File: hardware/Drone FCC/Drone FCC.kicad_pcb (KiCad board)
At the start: 2 copper layers, 80 x 62.2 mm, 36 parts, among them J1 Mag Dupont, J10 Conn_01x03, J11 Conn_01x03, J12 Conn_01x03, J13 Conn_01x03, J14 Conn_01x03, J17 Conn_01x03, J18 Conn_01x03, J19 GPS M8N - DF13, J2 GPS Dupont, J20 Mag DF13, J21 Micro_SD_Card_Det_Hirose_DM3AT, J22 Conn_02x03_Counter_Clockwise, J23 Conn_01x03, J24 DSM Spektrum JST, J25 105017-0001, J26 Conn_01x03, J27 PPM Dupont, J28 PM02 PixHawk, J3 Conn_01x03, J4 Conn_01x03, J5 Conn_01x03, J6 Conn_01x03, J7 Conn_01x03, J8 Conn_01x03, J9 Conn_01x03, SW1 SW_MEC_5E, U1 ICM-42688-V, U2 ILPS22QSTR, U3 STM32F746ZGTx, U4 SN65HVD230, U5 SN65HVD230, U6 ZLDO1117QG33TA, U7 USBLC6-2SC6

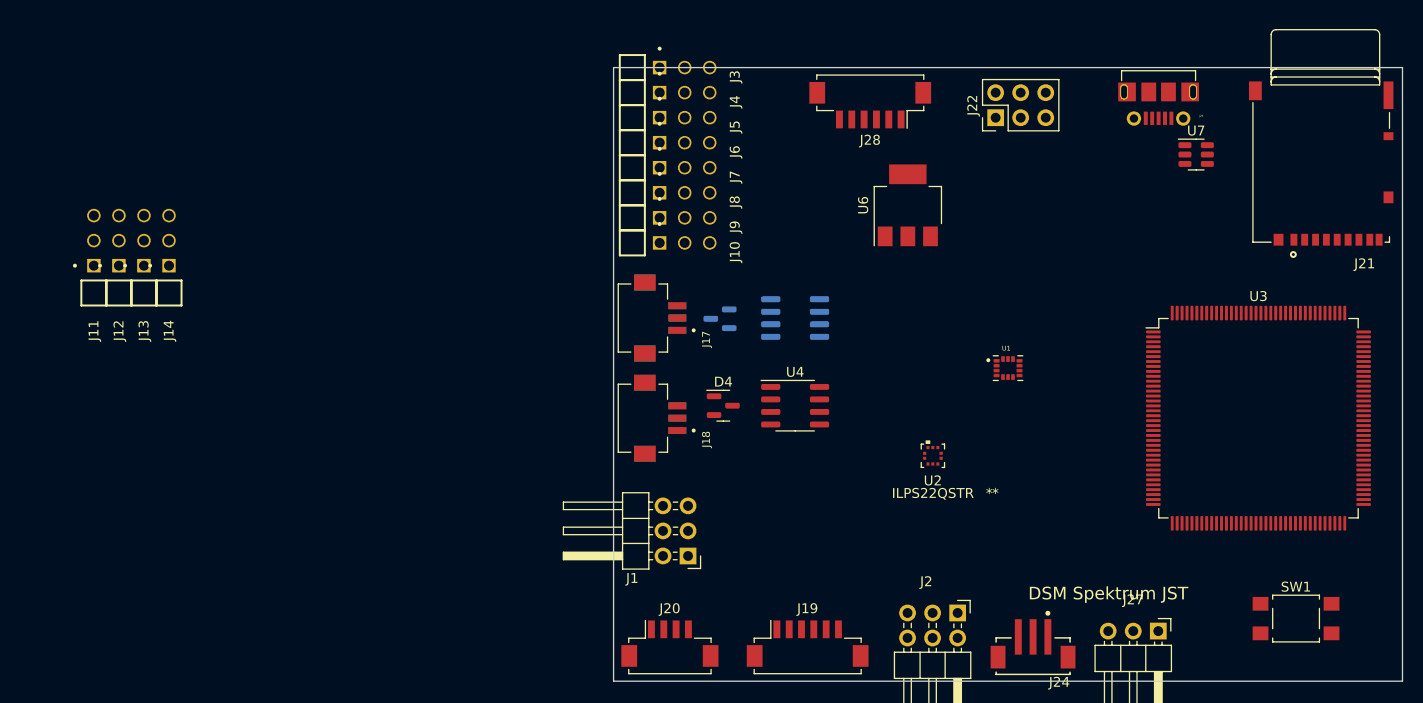
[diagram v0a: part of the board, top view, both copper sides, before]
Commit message: add external communication connectors
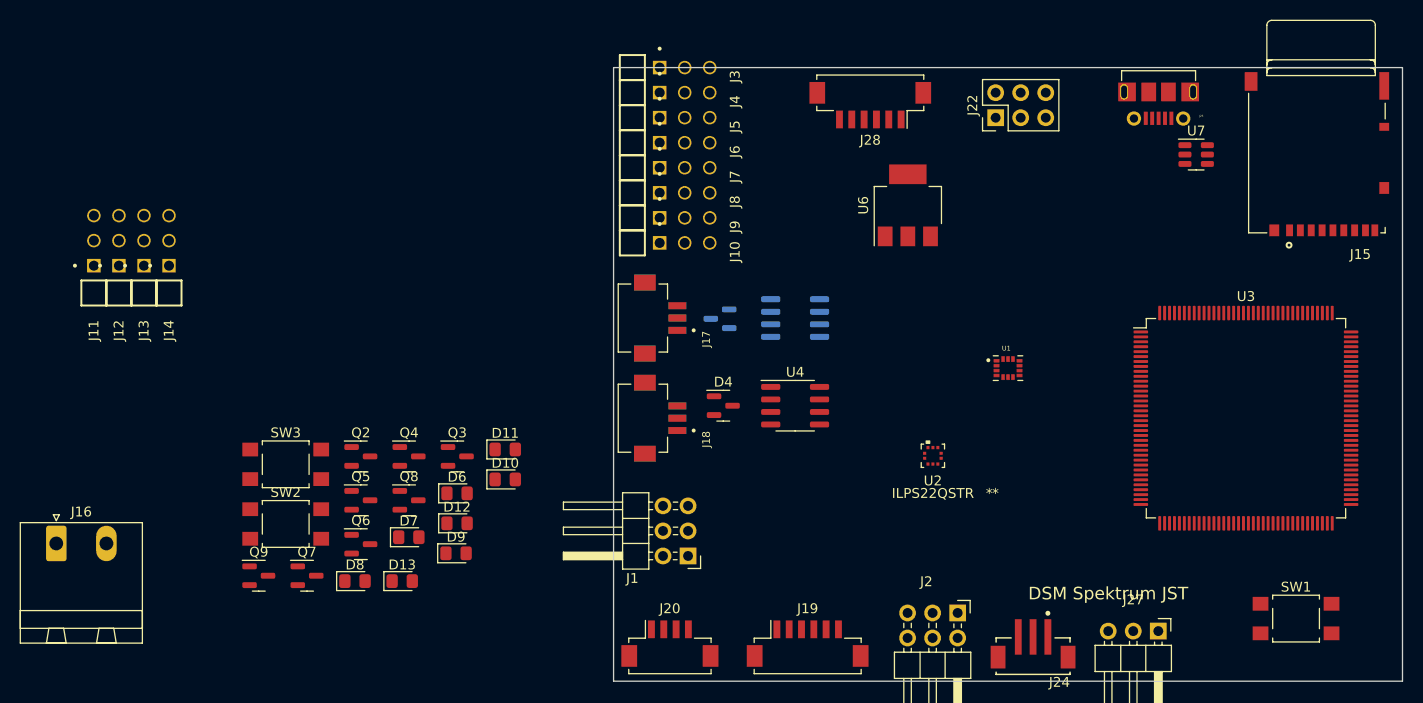
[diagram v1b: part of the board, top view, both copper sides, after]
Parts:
- removed J21: Micro_SD_Card_Det_Hirose_DM3AT, DM3AT-SF-PEJM5:HRS_DM3AT-SF-PEJM5
- added D10: LED_BLUE, LED_SMD:LED_0805_2012Metric_Pad1.15x1.40mm_HandSolder, F.Cu at (104.0, 101.5)
- added D11: LED_BLUE, LED_SMD:LED_0805_2012Metric_Pad1.15x1.40mm_HandSolder, F.Cu at (104.0, 98.4)
- added D12: LED_YELLOW, LED_SMD:LED_0805_2012Metric_Pad1.15x1.40mm_HandSolder, F.Cu at (99.1, 105.9)
- added D13: LED_YELLOW, LED_SMD:LED_0805_2012Metric_Pad1.15x1.40mm_HandSolder, F.Cu at (93.5, 111.8)
- added D6: LED_RED, LED_SMD:LED_0805_2012Metric_Pad1.15x1.40mm_HandSolder, F.Cu at (99.1, 102.9)
- added D7: LED_GREEN, LED_SMD:LED_0805_2012Metric_Pad1.15x1.40mm_HandSolder, F.Cu at (94.2, 107.3)
- added D8: LED_RED, LED_SMD:LED_0805_2012Metric_Pad1.15x1.40mm_HandSolder, F.Cu at (88.7, 111.8)
- added D9: LED_GREEN, LED_SMD:LED_0805_2012Metric_Pad1.15x1.40mm_HandSolder, F.Cu at (99.0, 109.0)
- added J15: DM3AT-SF-PEJM5, DM3AT-SF-PEJM5:HRS_DM3AT-SF-PEJM5, F.Cu at (186.7, 76.2)
- added J16: Conn_01x02, Connector_Phoenix_MSTB:PhoenixContact_MSTBA_2,5_2-G-5,08_1x02_P5.08mm_Horizontal, F.Cu at (58.4, 108.0)
- added Q2: 2N7002, Package_TO_SOT_SMD:SOT-23, F.Cu at (89.3, 99.1)
- added Q3: 2N7002, Package_TO_SOT_SMD:SOT-23, F.Cu at (99.1, 99.1)
- added Q4: 2N7002, Package_TO_SOT_SMD:SOT-23, F.Cu at (94.2, 99.1)
- added Q5: 2N7002, Package_TO_SOT_SMD:SOT-23, F.Cu at (89.3, 103.6)
- added Q6: 2N7002, Package_TO_SOT_SMD:SOT-23, F.Cu at (89.3, 108.0)
- added Q7: 2N7002, Package_TO_SOT_SMD:SOT-23, F.Cu at (83.8, 111.2)
- added Q8: 2N7002, Package_TO_SOT_SMD:SOT-23, F.Cu at (94.2, 103.6)
- added Q9: 2N7002, Package_TO_SOT_SMD:SOT-23, F.Cu at (79.0, 111.2)
- added SW2: SW_MEC_5E, Button_Switch_SMD:SW_SPST_TL3305A, F.Cu at (81.7, 106.0)
- added SW3: SW_MEC_5E, Button_Switch_SMD:SW_SPST_TL3305A, F.Cu at (81.7, 99.9)
- moved U3 1.27 mm to (179.1, 95.2)
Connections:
- J10 pad 1: /Motores_servos_PWM/ESC_8 -> /MCU/TIM4_CH4
- J11 pad 1: /Motores_servos_PWM/SERVO_1 -> /MCU/TIM1_CH1
- J12 pad 1: /Motores_servos_PWM/SERVO_2 -> /MCU/TIM1_CH2
- J13 pad 1: /Motores_servos_PWM/SERVO_3 -> /MCU/TIM1_CH3
- J14 pad 1: /Motores_servos_PWM/SERVO_4 -> /MCU/TIM1_CH4
- J2 pad 6: /Sensores/GNSS_PPS -> /MCU/PD_10(EXTI10)
- J24 pad 3: /RC control/DSM_DATA -> /MCU/USART6_RX
- J27 pad 3: /RC control/PPM -> /MCU/TIM2_CH3
- J3 pad 1: /MCU/PWM1 -> /MCU/TIM3_CH1
- J4 pad 1: /MCU/PWM2 -> /MCU/TIM3_CH2
- J5 pad 1: /MCU/PWM3 -> /MCU/TIM3_CH3
- J6 pad 1: /MCU/PWM4 -> /MCU/TIM3_CH4
- J7 pad 1: /MCU/PWM8 -> /MCU/TIM4_CH1
- J8 pad 1: /MCU/PWM9 -> /MCU/TIM4_CH2
- J9 pad 1: /Motores_servos_PWM/ESC_7 -> /MCU/TIM4_CH3
- U1 pad 1: /MCU/SPI1_MISO -> /MCU/SPI5_MISO
- U1 pad 12: /Sensores/IMU_CS -> /MCU/SPI5_CS
- U1 pad 13: /MCU/SPI1_SCK -> /MCU/SPI5_SCK
- U1 pad 14: /MCU/SPI1_MOSI -> /MCU/SPI5_MOSI
- U1 pad 4: /Sensores/IMU_INT_DATA_RDY -> /MCU/PF_5(EXTI5)
- U2 pad 2: /MCU/I2C2_SCL -> /Sensores/GNSS_SCL
- U2 pad 4: /MCU/I2C2_SDA -> /Sensores/GNSS_SDA
- U3 pad 114: /Interfaz_CAN/CAN1_RX -> unconnected-(U3-Pad114)
- U3 pad 115: /Interfaz_CAN/CAN1_TX -> unconnected-(U3-Pad115)
- U3 pad 118: unconnected-(U3-Pad118) -> /MCU/PD_4(EXTI4)
- U3 pad 124: unconnected-(U3-Pad124) -> /MCU/USART6_RX
- U3 pad 137: unconnected-(U3-Pad137) -> /Interfaz_CAN/CAN2_MODE
- U3 pad 139: unconnected-(U3-Pad139) -> /Interfaz_CAN/CAN1_RX
- U3 pad 140: unconnected-(U3-Pad140) -> /Interfaz_CAN/CAN1_TX
- U3 pad 141: unconnected-(U3-Pad141) -> /Interfaz_CAN/CAN1_MODE
- U3 pad 15: unconnected-(U3-Pad15) -> /MCU/PF_5(EXTI5)
- U3 pad 18: unconnected-(U3-Pad18) -> /MCU/SPI5_CS
- U3 pad 19: unconnected-(U3-Pad19) -> /MCU/SPI5_SCK
- U3 pad 20: unconnected-(U3-Pad20) -> /MCU/SPI5_MISO
- U3 pad 21: unconnected-(U3-Pad21) -> /MCU/SPI5_MOSI
- U3 pad 28: unconnected-(U3-Pad28) -> /Alimentación/I_MEAS
- U3 pad 29: unconnected-(U3-Pad29) -> /Alimentación/V_MEAS
- U3 pad 36: unconnected-(U3-Pad36) -> /MCU/TIM2_CH3
- U3 pad 41: /MCU/SPI1_SCK -> unconnected-(U3-Pad41)
- U3 pad 42: /MCU/SPI1_MISO -> /MCU/TIM3_CH1
- U3 pad 43: /MCU/SPI1_MOSI -> /MCU/TIM3_CH2
- U3 pad 46: unconnected-(U3-Pad46) -> /MCU/TIM3_CH3
- U3 pad 47: unconnected-(U3-Pad47) -> /MCU/TIM3_CH4
- U3 pad 53: /MCU/I2C4_SMBA -> unconnected-(U3-Pad53)
- U3 pad 56: unconnected-(U3-Pad56) -> /Sensores/MAG_INT_DATA_RDY
- U3 pad 60: /MCU/PWM11 -> /MCU/TIM1_CH1
- U3 pad 64: /MCU/PWM10 -> /MCU/TIM1_CH2
- U3 pad 66: /MCU/PWM9 -> /MCU/TIM1_CH3
- U3 pad 67: /MCU/PWM8 -> /MCU/TIM1_CH4
- U3 pad 68: unconnected-(U3-Pad68) -> /MCU/PE_15(EXTI15)
- U3 pad 69: /MCU/I2C2_SCL -> /Sensores/GNSS_SCL
- U3 pad 7: /MCU/SD_SW -> unconnected-(U3-Pad7)
- U3 pad 70: /MCU/I2C2_SDA -> /Sensores/GNSS_SDA
- U3 pad 77: unconnected-(U3-Pad77) -> /Sensores/GNSS_Tx
- U3 pad 78: unconnected-(U3-Pad78) -> /Sensores/GNSS_Rx
- U3 pad 79: unconnected-(U3-Pad79) -> /MCU/PD_10(EXTI10)
- U3 pad 81: /MCU/PWM1 -> /MCU/TIM4_CH1
- U3 pad 82: /MCU/PWM2 -> /MCU/TIM4_CH2
- U3 pad 85: /MCU/PWM3 -> /MCU/TIM4_CH3
- U3 pad 86: /MCU/PWM4 -> /MCU/TIM4_CH4

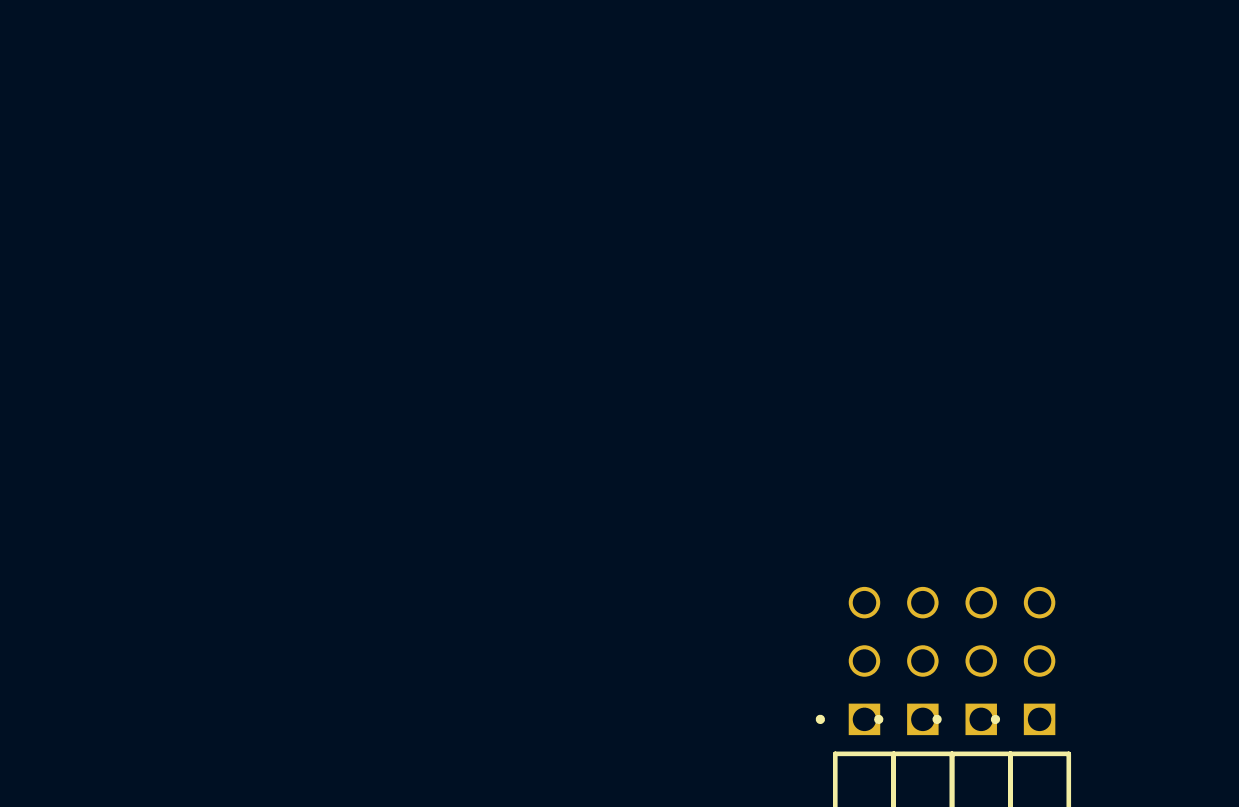
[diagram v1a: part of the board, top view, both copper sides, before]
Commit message: re enumeration of components
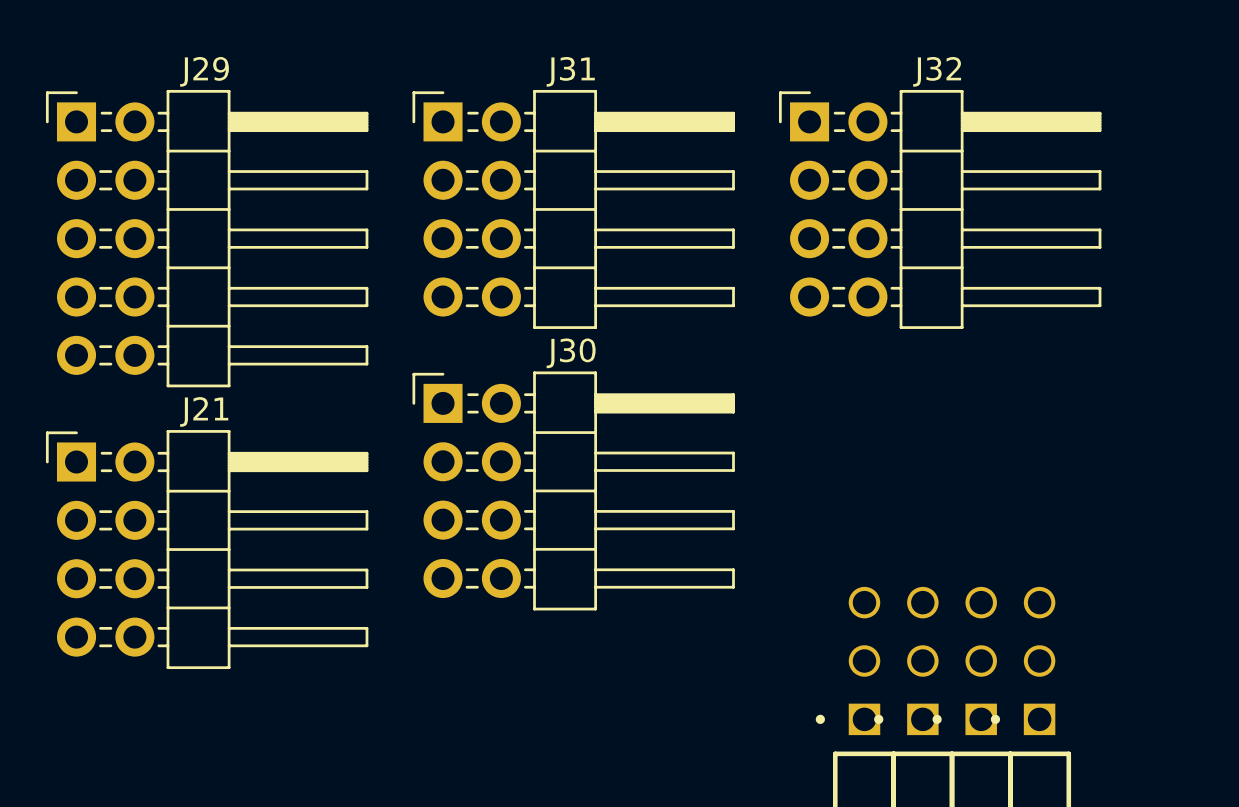
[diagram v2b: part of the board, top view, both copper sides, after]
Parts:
- added J21: SPI externo, Connector_PinHeader_2.54mm:PinHeader_2x04_P2.54mm_Horizontal, F.Cu at (27.9, 68.6)
- added J29: I2C externo x2, Connector_PinHeader_2.54mm:PinHeader_2x05_P2.54mm_Horizontal, F.Cu at (27.9, 53.8)
- added J30: UART externa x2, Connector_PinHeader_2.54mm:PinHeader_2x04_P2.54mm_Horizontal, F.Cu at (43.9, 66.0)
- added J31: UART externa x2, Connector_PinHeader_2.54mm:PinHeader_2x04_P2.54mm_Horizontal, F.Cu at (43.9, 53.8)
- added J32: 5V y 3V3 x 2, Connector_PinHeader_2.54mm:PinHeader_2x04_P2.54mm_Horizontal, F.Cu at (59.8, 53.8)
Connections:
- J24 pad 3: /MCU/USART6_RX -> /MCU/UART7_RX
- U3 pad 1: unconnected-(U3-Pad1) -> /Conexiones_extra/SPI_SCK
- U3 pad 110: unconnected-(U3-Pad110) -> /Interfaz_CAN/CAN1_MODE
- U3 pad 114: unconnected-(U3-Pad114) -> /Interfaz_CAN/CAN1_RX
- U3 pad 115: unconnected-(U3-Pad115) -> /Interfaz_CAN/CAN1_TX
- U3 pad 119: unconnected-(U3-Pad119) -> /Conexiones_extra/UARTB_TX
- U3 pad 122: unconnected-(U3-Pad122) -> /Conexiones_extra/UARTB_RX
- U3 pad 124: /MCU/USART6_RX -> /Conexiones_extra/UARTA_RX
- U3 pad 129: unconnected-(U3-Pad129) -> /Conexiones_extra/UARTA_TX
- U3 pad 139: /Interfaz_CAN/CAN1_RX -> /Conexiones_extra/I2CA_SCL
- U3 pad 140: /Interfaz_CAN/CAN1_TX -> /Conexiones_extra/I2CA_SDA
- U3 pad 141: /Interfaz_CAN/CAN1_MODE -> /Conexiones_extra/UARTD_RX
- U3 pad 142: unconnected-(U3-Pad142) -> /Conexiones_extra/UARTD_TX
- U3 pad 2: unconnected-(U3-Pad2) -> /Conexiones_extra/SPI_EOC
- U3 pad 3: unconnected-(U3-Pad3) -> /Conexiones_extra/SPI_CS
- U3 pad 34: unconnected-(U3-Pad34) -> /Conexiones_extra/UARTC_TX
- U3 pad 35: unconnected-(U3-Pad35) -> /Conexiones_extra/UARTC_RX
- U3 pad 4: unconnected-(U3-Pad4) -> /Conexiones_extra/SPI_MISO
- U3 pad 5: unconnected-(U3-Pad5) -> /Conexiones_extra/SPI_MOSI
- U3 pad 58: unconnected-(U3-Pad58) -> /MCU/UART7_RX

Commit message: start routing
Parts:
- removed J17, J18, J23, J26: Conn_01x03, DF13A-3P-1.25H(21):HRS_DF13A-3P-1.25H(21)
- removed J19: GPS M8N - DF13, Connector_Hirose:Hirose_DF13C_CL535-0406-3-51_1x06-1MP_P1.25mm_Vertical
- removed J20: Mag DF13, Connector_Hirose:Hirose_DF13C_CL535-0404-8-51_1x04-1MP_P1.25mm_Vertical
- removed J24: DSM Spektrum JST, B3B-ZR-SM4-TF(LF)(SN):JST-B3B-ZR-SM4-TFLFSN-0-0-MFG
- removed J25: 105017-0001, 105017-0001:MOLEX_105017-0001
- removed J28: PM02 PixHawk, Connector_Hirose:Hirose_DF13C_CL535-0406-3-51_1x06-1MP_P1.25mm_Vertical
- removed SW1, SW2, SW3: SW_MEC_5E, Button_Switch_SMD:SW_SPST_TL3305A
- added C101: 100nF, Capacitor_SMD:C_0603_1608Metric_Pad1.08x0.95mm_HandSolder, F.Cu at (-57.1, 163.8)
- added C102: 100nF, Capacitor_SMD:C_0603_1608Metric_Pad1.08x0.95mm_HandSolder, F.Cu at (-76.4, 178.4)
- added C103: 1uF, Capacitor_SMD:C_0805_2012Metric_Pad1.18x1.45mm_HandSolder, F.Cu at (-61.3, 161.1)
- added C104: 100nF, Capacitor_SMD:C_0603_1608Metric_Pad1.08x0.95mm_HandSolder, F.Cu at (-61.5, 163.8)
- added C105: 100nF, Capacitor_SMD:C_0603_1608Metric_Pad1.08x0.95mm_HandSolder, F.Cu at (230.0, 75.4)
- added C106: 100nF, Capacitor_SMD:C_0603_1608Metric_Pad1.08x0.95mm_HandSolder, F.Cu at (-72.1, 170.2)
- added C107: 100nF, Capacitor_SMD:C_0603_1608Metric_Pad1.08x0.95mm_HandSolder, F.Cu at (-62.9, 166.3)
- added C108: 100nF, Capacitor_SMD:C_0603_1608Metric_Pad1.08x0.95mm_HandSolder, F.Cu at (-62.9, 168.8)
- added C109: 100nF, Capacitor_SMD:C_0603_1608Metric_Pad1.08x0.95mm_HandSolder, F.Cu at (-67.3, 167.8)
- added C110: 100nF, Capacitor_SMD:C_0603_1608Metric_Pad1.08x0.95mm_HandSolder, F.Cu at (-72.1, 175.2)
- added C1101: 100nF, Capacitor_SMD:C_0402_1005Metric_Pad0.74x0.62mm_HandSolder, F.Cu at (-24.7, 192.5)
- added C1102: 100nF, Capacitor_SMD:C_0402_1005Metric_Pad0.74x0.62mm_HandSolder, F.Cu at (-18.4, 186.6)
- added C111: 100nF, Capacitor_SMD:C_0603_1608Metric_Pad1.08x0.95mm_HandSolder, F.Cu at (-67.3, 165.3)
- added C112: 100nF, Capacitor_SMD:C_0603_1608Metric_Pad1.08x0.95mm_HandSolder, F.Cu at (-67.8, 170.3)
- added C113: 100nF, Capacitor_SMD:C_0603_1608Metric_Pad1.08x0.95mm_HandSolder, F.Cu at (-67.8, 172.8)
- added C114: 100nF, Capacitor_SMD:C_0603_1608Metric_Pad1.08x0.95mm_HandSolder, F.Cu at (-52.3, 160.8)
- added C115: 100nF, Capacitor_SMD:C_0603_1608Metric_Pad1.08x0.95mm_HandSolder, F.Cu at (-56.7, 160.8)
- added C116: 4.7uF, Capacitor_SMD:C_0805_2012Metric_Pad1.18x1.45mm_HandSolder, F.Cu at (-72.9, 164.4)
- added C117: 2.2uF, Capacitor_SMD:C_1206_3216Metric_Pad1.33x1.80mm_HandSolder, F.Cu at (-81.6, 178.8)
- added C118: 2.2uF, Capacitor_SMD:C_1206_3216Metric_Pad1.33x1.80mm_HandSolder, F.Cu at (-72.3, 161.2)
- added C119: 100nF, Capacitor_SMD:C_0603_1608Metric_Pad1.08x0.95mm_HandSolder, F.Cu at (-72.1, 172.7)
- added C120: 6pF, Capacitor_SMD:C_0402_1005Metric_Pad0.74x0.62mm_HandSolder, F.Cu at (199.8, 132.3)
- added C121: 6pF, Capacitor_SMD:C_0402_1005Metric_Pad0.74x0.62mm_HandSolder, F.Cu at (199.8, 135.0)
- added C122: 8pF, Capacitor_SMD:C_0402_1005Metric_Pad0.74x0.62mm_HandSolder, F.Cu at (198.3, 118.3)
- added C123: 8pF, Capacitor_SMD:C_0402_1005Metric_Pad0.74x0.62mm_HandSolder, F.Cu at (198.3, 120.8)
- added C124: 1uF, Capacitor_SMD:C_0805_2012Metric_Pad1.18x1.45mm_HandSolder, F.Cu at (-71.9, 167.4)
- added C201: 10n, Capacitor_SMD:C_0603_1608Metric_Pad1.08x0.95mm_HandSolder, F.Cu at (-23.2, 160.8)
- added C202: 0.1u, Capacitor_SMD:C_0603_1608Metric_Pad1.08x0.95mm_HandSolder, F.Cu at (-30.2, 168.3)
- added C203: 2.2u, Capacitor_SMD:C_0603_1608Metric_Pad1.08x0.95mm_HandSolder, F.Cu at (-42.1, 175.6)
- added C204: 0.1u, Capacitor_SMD:C_0603_1608Metric_Pad1.08x0.95mm_HandSolder, F.Cu at (-37.7, 175.6)
- added C205: 0.1u, Capacitor_SMD:C_0603_1608Metric_Pad1.08x0.95mm_HandSolder, F.Cu at (-28.0, 163.8)
- added C206: 4.7u, Capacitor_SMD:C_0805_2012Metric_Pad1.18x1.45mm_HandSolder, F.Cu at (-27.7, 161.1)
- added C701: 100nF, Capacitor_SMD:C_0603_1608Metric_Pad1.08x0.95mm_HandSolder, F.Cu at (266.4, 40.0)
- added C702: 10uF, Capacitor_SMD:C_0603_1608Metric_Pad1.08x0.95mm_HandSolder, F.Cu at (266.4, 42.5)
- added C801: 2.2u, Capacitor_SMD:C_0603_1608Metric_Pad1.08x0.95mm_HandSolder, F.Cu at (-61.8, 187.3)
- added C802: 100nF, Capacitor_SMD:C_0603_1608Metric_Pad1.08x0.95mm_HandSolder, F.Cu at (-57.4, 184.8)
- added C803: 100nF, Capacitor_SMD:C_0402_1005Metric_Pad0.74x0.62mm_HandSolder, F.Cu at (-55.8, 189.6)
- added C804: 2.2u, Capacitor_SMD:C_0603_1608Metric_Pad1.08x0.95mm_HandSolder, F.Cu at (-61.8, 184.8)
- added C805: 100nF, Capacitor_SMD:C_0603_1608Metric_Pad1.08x0.95mm_HandSolder, F.Cu at (-57.4, 187.3)
- added C806: 100nF, Capacitor_SMD:C_0402_1005Metric_Pad0.74x0.62mm_HandSolder, F.Cu at (-59.1, 193.6)
- added C901: 1.6u, Capacitor_SMD:C_0603_1608Metric_Pad1.08x0.95mm_HandSolder, F.Cu at (11.6, 160.8)
- added C902: 0.1u, Capacitor_SMD:C_0603_1608Metric_Pad1.08x0.95mm_HandSolder, F.Cu at (1.68, 173.3)
- added C903: 10u, Capacitor_SMD:C_0805_2012Metric_Pad1.18x1.45mm_HandSolder, F.Cu at (6.31, 164.3)
- added C904: 10u, Capacitor_SMD:C_0805_2012Metric_Pad1.18x1.45mm_HandSolder, F.Cu at (-2.90, 171.8)
- added C905: 100n, Capacitor_SMD:C_0603_1608Metric_Pad1.08x0.95mm_HandSolder, F.Cu at (2.92, 170.8)
- added C906: 100p, Capacitor_SMD:C_0402_1005Metric_Pad0.74x0.62mm_HandSolder, F.Cu at (14.7, 163.1)
- added C907: 100p, Capacitor_SMD:C_0402_1005Metric_Pad0.74x0.62mm_HandSolder, F.Cu at (6.70, 170.8)
- added D901: PMEG60T30ELRX, PMEG60T30ELRX:SODFL3517X110N, F.Cu at (6.64, 161.2)
- added D902: PMEG60T30ELRX, PMEG60T30ELRX:SODFL3517X110N, F.Cu at (-1.99, 168.7)
- added D903: PMEG60T30ELRX, PMEG60T30ELRX:SODFL3517X110N, F.Cu at (237.3, 106.3)
- added D903: PMEG60T30ELRX, PMEG60T30ELRX:SODFL3517X110N, F.Cu at (446.1, 91.2)
- added J1001: SPI externo, Connector_PinHeader_2.54mm:PinHeader_2x04_P2.54mm_Horizontal, F.Cu at (384.6, 132.7)
- added J1002: UART externa x2, Connector_PinHeader_2.54mm:PinHeader_2x04_P2.54mm_Horizontal, F.Cu at (384.6, 112.4)
- added J1003: I2C externo x2, Connector_PinHeader_2.54mm:PinHeader_2x05_P2.54mm_Horizontal, F.Cu at (398.0, 154.7)
- added J1004: UART externa x2, Connector_PinHeader_2.54mm:PinHeader_2x04_P2.54mm_Horizontal, F.Cu at (384.6, 122.5)
- added J1005: 5V y 3V3 x 2, Connector_PinHeader_2.54mm:PinHeader_2x04_P2.54mm_Horizontal, F.Cu at (433.2, 89.1)
- added J201: Mag Dupont, Connector_PinHeader_2.54mm:PinHeader_2x03_P2.54mm_Horizontal, F.Cu at (450.3, 137.9)
- added J202: Mag DF13, Connector_Hirose:Hirose_DF13C_CL535-0404-8-51_1x04-1MP_P1.25mm_Vertical, F.Cu at (221.6, 152.7)
- added J202: Mag DF13, Connector_Hirose:Hirose_DF13C_CL535-0404-8-51_1x04-1MP_P1.25mm_Vertical, F.Cu at (453.1, 151.1)
- added J203: GPS Dupont, Connector_PinHeader_2.54mm:PinHeader_2x03_P2.54mm_Horizontal, F.Cu at (450.3, 130.3)
- added J204: GPS M8N - DF13, DF13C-6P-1.25V(51):HIROSE_DF13C-6P-1.25V(51), F.Cu at (246.1, 134.7)
- added J204: GPS M8N - DF13, DF13C-6P-1.25V(51):HIROSE_DF13C-6P-1.25V(51), F.Cu at (454.1, 120.5)
- added J301: ESC 1, TSW-101-08-G-T-RA:SAMTEC_TSW-101-08-G-T-RA, F.Cu at (426.1, 160.2)
- added J302: ESC 2, TSW-101-08-G-T-RA:SAMTEC_TSW-101-08-G-T-RA, F.Cu at (428.7, 160.2)
- added J303: ESC 3, TSW-101-08-G-T-RA:SAMTEC_TSW-101-08-G-T-RA, F.Cu at (431.2, 160.2)
- added J304: ESC 4, TSW-101-08-G-T-RA:SAMTEC_TSW-101-08-G-T-RA, F.Cu at (433.7, 160.2)
- added J305: ESC 5, TSW-101-08-G-T-RA:SAMTEC_TSW-101-08-G-T-RA, F.Cu at (436.3, 160.2)
- added J306: ESC 6, TSW-101-08-G-T-RA:SAMTEC_TSW-101-08-G-T-RA, F.Cu at (438.8, 160.2)
- added J307: ESC 7, TSW-101-08-G-T-RA:SAMTEC_TSW-101-08-G-T-RA, F.Cu at (441.4, 160.2)
- added J308: ESC 8, TSW-101-08-G-T-RA:SAMTEC_TSW-101-08-G-T-RA, F.Cu at (443.9, 160.2)
- added J309: SERVO 1, TSW-101-08-G-T-RA:SAMTEC_TSW-101-08-G-T-RA, F.Cu at (400.6, 160.2)
- added J310: SERVO 2, TSW-101-08-G-T-RA:SAMTEC_TSW-101-08-G-T-RA, F.Cu at (403.1, 160.2)
- added J311: SERVO 3, TSW-101-08-G-T-RA:SAMTEC_TSW-101-08-G-T-RA, F.Cu at (405.7, 160.2)
- added J312: SERVO 4, TSW-101-08-G-T-RA:SAMTEC_TSW-101-08-G-T-RA, F.Cu at (408.2, 160.2)
- added J313: Power Servo, Connector_Phoenix_MSTB:PhoenixContact_MSTBA_2,5_2-G-5,08_1x02_P5.08mm_Horizontal, F.Cu at (414.4, 151.2)
- added J401: DSM Spektrum JST, B3B-ZR-SM4-TF(LF)(SN):JST-B3B-ZR-SM4-TFLFSN-0-0-MFG, F.Cu at (379.7, 140.6)
- added J401: DSM Spektrum JST, B3B-ZR-SM4-TF(LF)(SN):JST-B3B-ZR-SM4-TFLFSN-0-0-MFG, F.Cu at (196.6, 154.1)
- added J402: PPM Dupont, Connector_PinHeader_2.54mm:PinHeader_1x03_P2.54mm_Horizontal, F.Cu at (382.0, 153.2)
- added J501: Micro USB - B, 105017-0001:MOLEX_105017-0001, F.Cu at (454.5, 108.7)
- added J501: Micro USB - B, 105017-0001:MOLEX_105017-0001, F.Cu at (246.0, 122.7)
- added J601: SWD Debug Connector, Connector_PinHeader_2.54mm:PinHeader_2x03_P2.54mm_Vertical, F.Cu at (486.6, 105.8)
- added J701: DM3AT-SF-PEJM5, DM3AT-SF-PEJM5:HRS_DM3AT-SF-PEJM5, F.Cu at (417.8, 99.5)
- added J801: CAN 1 Connector 1, DF13A-3P-1.25H(21):HRS_DF13A-3P-1.25H(21), F.Cu at (390.5, 85.6)
- added J801: CAN 1 Connector 1, DF13A-3P-1.25H(21):HRS_DF13A-3P-1.25H(21), F.Cu at (168.3, 100.3)
- added J802: CAN 1 Connector 2, DF13A-3P-1.25H(21):HRS_DF13A-3P-1.25H(21), F.Cu at (400.3, 85.5)
- added J802: CAN 1 Connector 2, DF13A-3P-1.25H(21):HRS_DF13A-3P-1.25H(21), F.Cu at (178.4, 100.3)
- added J803: CAN 2 Connector 1, DF13A-3P-1.25H(21):HRS_DF13A-3P-1.25H(21), B.Cu at (400.7, 85.8)
- added J803: CAN 2 Connector 1, DF13A-3P-1.25H(21):HRS_DF13A-3P-1.25H(21), B.Cu at (180.5, 100.0)
- added J804: CAN 2 Connector 2, DF13A-3P-1.25H(21):HRS_DF13A-3P-1.25H(21), B.Cu at (165.0, 100.1)
- added J804: CAN 2 Connector 2, DF13A-3P-1.25H(21):HRS_DF13A-3P-1.25H(21), B.Cu at (390.8, 85.9)
- added J901: PM02 PixHawk, DF13C-6P-1.25V(51):HIROSE_DF13C-6P-1.25V(51), F.Cu at (245.7, 109.9)
- added J901: PM02 PixHawk, DF13C-6P-1.25V(51):HIROSE_DF13C-6P-1.25V(51), F.Cu at (454.4, 95.3)
- added Q901: Q_PMOS_GSD, Package_TO_SOT_SMD:SOT-23, F.Cu at (-7.75, 172.5)
- added R101: R, Resistor_SMD:R_0402_1005Metric_Pad0.72x0.64mm_HandSolder, F.Cu at (-59.1, 170.1)
- added R102: R, Resistor_SMD:R_0402_1005Metric_Pad0.72x0.64mm_HandSolder, F.Cu at (-59.1, 166.1)
- added R103: R, Resistor_SMD:R_0402_1005Metric_Pad0.72x0.64mm_HandSolder, F.Cu at (-53.4, 163.1)
- added R104: R, Resistor_SMD:R_0402_1005Metric_Pad0.72x0.64mm_HandSolder, F.Cu at (-64.0, 173.1)
- added R105: R, Resistor_SMD:R_0402_1005Metric_Pad0.72x0.64mm_HandSolder, F.Cu at (-68.3, 177.0)
- added R106: R, Resistor_SMD:R_0402_1005Metric_Pad0.72x0.64mm_HandSolder, F.Cu at (-59.1, 168.1)
- added R107: 10k, Resistor_SMD:R_0402_1005Metric_Pad0.72x0.64mm_HandSolder, F.Cu at (-55.9, 166.1)
- added R108: 10k, Resistor_SMD:R_0402_1005Metric_Pad0.72x0.64mm_HandSolder, F.Cu at (-68.3, 179.0)
- added R109: 10k, Resistor_SMD:R_0402_1005Metric_Pad0.72x0.64mm_HandSolder, F.Cu at (-64.0, 171.1)
- added R110: 0, Resistor_SMD:R_0402_1005Metric_Pad0.72x0.64mm_HandSolder, F.Cu at (-55.9, 168.1)
- added R1101: R, Resistor_SMD:R_0402_1005Metric_Pad0.72x0.64mm_HandSolder, F.Cu at (-21.6, 187.5)
- added R1102: R, Resistor_SMD:R_0402_1005Metric_Pad0.72x0.64mm_HandSolder, F.Cu at (-34.4, 193.4)
- added R1103: R, Resistor_SMD:R_0805_2012Metric_Pad1.20x1.40mm_HandSolder, F.Cu at (-33.6, 185.1)
- added R1104: R, Resistor_SMD:R_0402_1005Metric_Pad0.72x0.64mm_HandSolder, F.Cu at (-44.8, 199.6)
- added R1105: R, Resistor_SMD:R_0402_1005Metric_Pad0.72x0.64mm_HandSolder, F.Cu at (-31.1, 193.4)
- added R1106: R, Resistor_SMD:R_0805_2012Metric_Pad1.20x1.40mm_HandSolder, F.Cu at (-33.6, 191.0)
- added R1107: R, Resistor_SMD:R_0402_1005Metric_Pad0.72x0.64mm_HandSolder, F.Cu at (-32.0, 195.4)
- added R1108: R, Resistor_SMD:R_0402_1005Metric_Pad0.72x0.64mm_HandSolder, F.Cu at (-27.9, 194.5)
- added R1109: R, Resistor_SMD:R_0805_2012Metric_Pad1.20x1.40mm_HandSolder, F.Cu at (-33.6, 188.0)
- added R111: 33k, Resistor_SMD:R_0402_1005Metric_Pad0.72x0.64mm_HandSolder, F.Cu at (-65.0, 175.1)
- added R1110: R, Resistor_SMD:R_0402_1005Metric_Pad0.72x0.64mm_HandSolder, F.Cu at (-31.8, 199.4)
- added R1111: R, Resistor_SMD:R_0402_1005Metric_Pad0.72x0.64mm_HandSolder, F.Cu at (-41.5, 199.6)
- added R1112: R, Resistor_SMD:R_0805_2012Metric_Pad1.20x1.40mm_HandSolder, F.Cu at (-28.9, 188.0)
- added R1113: R, Resistor_SMD:R_0402_1005Metric_Pad0.72x0.64mm_HandSolder, F.Cu at (-38.2, 199.6)
- added R1114: R, Resistor_SMD:R_0402_1005Metric_Pad0.72x0.64mm_HandSolder, F.Cu at (-27.9, 192.5)
- added R1115: R, Resistor_SMD:R_0805_2012Metric_Pad1.20x1.40mm_HandSolder, F.Cu at (-24.1, 185.1)
- added R1116: R, Resistor_SMD:R_0402_1005Metric_Pad0.72x0.64mm_HandSolder, F.Cu at (-35.2, 196.7)
- added R1117: R, Resistor_SMD:R_0402_1005Metric_Pad0.72x0.64mm_HandSolder, F.Cu at (-29.6, 190.5)
- added R1118: R, Resistor_SMD:R_0805_2012Metric_Pad1.20x1.40mm_HandSolder, F.Cu at (-44.0, 197.2)
- added R1119: R, Resistor_SMD:R_0402_1005Metric_Pad0.72x0.64mm_HandSolder, F.Cu at (-24.9, 187.5)
- added R112: 82k, Resistor_SMD:R_0402_1005Metric_Pad0.72x0.64mm_HandSolder, F.Cu at (-68.3, 175.1)
- added R1120: R, Resistor_SMD:R_0402_1005Metric_Pad0.72x0.64mm_HandSolder, F.Cu at (-20.1, 184.6)
- added R1121: R, Resistor_SMD:R_0805_2012Metric_Pad1.20x1.40mm_HandSolder, F.Cu at (-39.2, 197.2)
- added R1122: R, Resistor_SMD:R_0402_1005Metric_Pad0.72x0.64mm_HandSolder, F.Cu at (-35.0, 198.7)
- added R1123: R, Resistor_SMD:R_0402_1005Metric_Pad0.72x0.64mm_HandSolder, F.Cu at (-26.4, 190.5)
- added R1124: R, Resistor_SMD:R_0805_2012Metric_Pad1.20x1.40mm_HandSolder, F.Cu at (-28.9, 185.1)
- added R1125: R, Resistor_SMD:R_0402_1005Metric_Pad0.72x0.64mm_HandSolder, F.Cu at (-23.1, 189.5)
- added R1126: R, Resistor_SMD:R_0402_1005Metric_Pad0.72x0.64mm_HandSolder, F.Cu at (-31.8, 197.4)
- added R701: 10k, Resistor_SMD:R_0402_1005Metric_Pad0.72x0.64mm_HandSolder, F.Cu at (224.5, 56.7)
- added R702: 10k, Resistor_SMD:R_0402_1005Metric_Pad0.72x0.64mm_HandSolder, F.Cu at (227.8, 54.7)
- added R703: 10k, Resistor_SMD:R_0402_1005Metric_Pad0.72x0.64mm_HandSolder, F.Cu at (227.8, 52.7)
- added R704: 10k, Resistor_SMD:R_0402_1005Metric_Pad0.72x0.64mm_HandSolder, F.Cu at (224.5, 52.7)
- added R705: 10k, Resistor_SMD:R_0402_1005Metric_Pad0.72x0.64mm_HandSolder, F.Cu at (224.5, 54.7)
- added R706: 10k, Resistor_SMD:R_0402_1005Metric_Pad0.72x0.64mm_HandSolder, F.Cu at (227.8, 56.7)
- added R801: 220, Resistor_SMD:R_0402_1005Metric_Pad0.72x0.64mm_HandSolder, F.Cu at (244.7, 86.1)
- added R802: 220, Resistor_SMD:R_0402_1005Metric_Pad0.72x0.64mm_HandSolder, F.Cu at (-62.3, 195.6)
- added R803: 5.1k, Resistor_SMD:R_0402_1005Metric_Pad0.72x0.64mm_HandSolder, F.Cu at (-53.6, 186.6)
- added R804: 5.1k, Resistor_SMD:R_0402_1005Metric_Pad0.72x0.64mm_HandSolder, F.Cu at (-59.0, 189.6)
- added R805: 220, Resistor_SMD:R_0402_1005Metric_Pad0.72x0.64mm_HandSolder, F.Cu at (-62.3, 191.6)
- added R806: 220, Resistor_SMD:R_0402_1005Metric_Pad0.72x0.64mm_HandSolder, F.Cu at (-53.6, 184.6)
- added R807: 5.1k, Resistor_SMD:R_0402_1005Metric_Pad0.72x0.64mm_HandSolder, F.Cu at (-59.0, 191.6)
- added R808: 5.1k, Resistor_SMD:R_0402_1005Metric_Pad0.72x0.64mm_HandSolder, F.Cu at (-62.3, 193.6)
- added R901: 10, Resistor_SMD:R_0603_1608Metric_Pad0.98x0.95mm_HandSolder, F.Cu at (2.92, 168.3)
- added R902: 6.8k, Resistor_SMD:R_0603_1608Metric_Pad0.98x0.95mm_HandSolder, F.Cu at (15.9, 160.8)
- added R903: 33, Resistor_SMD:R_0603_1608Metric_Pad0.98x0.95mm_HandSolder, F.Cu at (10.9, 164.1)
- added R904: 1M, Resistor_SMD:R_0402_1005Metric_Pad0.72x0.64mm_HandSolder, F.Cu at (6.72, 166.8)
- added R905: 1M, Resistor_SMD:R_0402_1005Metric_Pad0.72x0.64mm_HandSolder, F.Cu at (-3.68, 174.3)
- added R906: 10k, Resistor_SMD:R_0402_1005Metric_Pad0.72x0.64mm_HandSolder, F.Cu at (6.72, 168.8)
- added R907: 10k, Resistor_SMD:R_0402_1005Metric_Pad0.72x0.64mm_HandSolder, F.Cu at (10.3, 166.3)
- added SW101: SW RESET, Button_Switch_SMD:SW_SPST_TL3305A, F.Cu at (-79.5, 174.1)
- added SW1101: SW Propósito General, Button_Switch_SMD:SW_SPST_TL3305A, F.Cu at (-41.2, 192.7)
- added SW1102: SW Propósito General, Button_Switch_SMD:SW_SPST_TL3305A, F.Cu at (-41.2, 186.6)
- added U101: STM32F746ZGTx, Package_QFP:LQFP-144_20x20mm_P0.5mm, F.Cu at (436.1, 110.9)
- added U201: ICM-42688-V, ICM-42688-V:PQFN50P300X250X97-14N, F.Cu at (417.3, 121.7)
- added U501: USBLC6-2SC6, Package_TO_SOT_SMD:SOT-23-6, F.Cu at (447.5, 109.1)
- added U801: SN65HVD230, Package_SO:SOIC-8_3.9x4.9mm_P1.27mm, F.Cu at (392.0, 95.4)
- added U802: SN65HVD230, Package_SO:SOIC-8_3.9x4.9mm_P1.27mm, B.Cu at (395.2, 95.2)
- added U901: ZLDO1117QG33TA, Package_TO_SOT_SMD:SOT-223-3_TabPin2, F.Cu at (434.1, 96.6)
- added Y101: 12MHz, ECS-120-8-33Q-RES-TR:XTAL_ECS-120-8-33Q-RES-TR, F.Cu at (195.8, 133.7)
- added Y102: 32.768kHz, ECS-.327-9-34QCS-TR9:ECS-.327-9-34QN-TR, F.Cu at (200.7, 119.6)
- J301: renamed from J3; value Conn_01x03 -> ESC 1
- J302: renamed from J4; value Conn_01x03 -> ESC 2
- J303: renamed from J5; value Conn_01x03 -> ESC 3
- J304: renamed from J6; value Conn_01x03 -> ESC 4
- J305: renamed from J7; value Conn_01x03 -> ESC 5
- J306: renamed from J8; value Conn_01x03 -> ESC 6
- J307: renamed from J9; value Conn_01x03 -> ESC 7
- J308: renamed from J10; value Conn_01x03 -> ESC 8
- J309: renamed from J11; value Conn_01x03 -> SERVO 1
- J310: renamed from J12; value Conn_01x03 -> SERVO 2
- J311: renamed from J13; value Conn_01x03 -> SERVO 3
- J312: renamed from J14; value Conn_01x03 -> SERVO 4
- J313: renamed from J16; value Conn_01x02 -> Power Servo
- J601: renamed from J22; value Conn_02x03_Counter_Clockwise -> SWD Debug Connector
- J701: renamed from J15; moved to B.Cu
- moved D1101 250.9 mm to (-157.7, 64.3)
- moved D1102 250.9 mm to (-147.3, 55.4)
- moved D1103 250.9 mm to (-152.2, 59.8)
- moved D1104 250.9 mm to (-147.4, 61.5)
- moved D1105 250.9 mm to (-147.3, 58.4)
- moved D1106 250.9 mm to (-152.9, 64.3)
- moved D1107 250.9 mm to (-142.4, 54.0)
- moved D1108 250.9 mm to (-142.4, 50.9)
- moved D801 250.9 mm to (-120.3, 46.5)
- moved D802 250.9 mm to (-120.7, 37.7)
- moved Q1101 250.9 mm to (-157.1, 51.6)
- moved Q1102 250.9 mm to (-157.1, 56.1)
- moved Q1103 250.9 mm to (-157.1, 60.5)
- moved Q1104 250.9 mm to (-152.2, 56.1)
- moved Q1105 250.9 mm to (-147.3, 51.6)
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- renumbered D8 to D1101, D6 to D1102, D7 to D1103, D9 to D1104, D12 to D1105, D13 to D1106, D10 to D1107, D11 to D1108, D4 to D801, D5 to D802, J21 to J1001, J30 to J1002, J29 to J1003, J31 to J1004, J32 to J1005, J1 to J201, J2 to J203, J27 to J402, Q2 to Q1101, Q5 to Q1102, Q6 to Q1103, Q8 to Q1104, Q3 to Q1105, Q4 to Q1106, Q7 to Q1107, Q9 to Q1108, U3 to U101, U1 to U201, U2 to U202, U7 to U501, U4 to U801, U5 to U802, U6 to U901
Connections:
- J201 pad 5: /Sensores/MAG_SCL -> /Sensores/GNSS_SCL
- J201 pad 6: /Sensores/MAG_SDA -> /Sensores/GNSS_SDA
- U101 pad 110: /Interfaz_CAN/CAN1_MODE -> unconnected-(U101-Pad110)
- U101 pad 114: /Interfaz_CAN/CAN1_RX -> unconnected-(U101-Pad114)
- U101 pad 115: /Interfaz_CAN/CAN1_TX -> unconnected-(U101-Pad115)
- U101 pad 134: unconnected-(U3-Pad134) -> /Interfaz_CAN/CAN2_MODE
- U101 pad 137: /Interfaz_CAN/CAN2_MODE -> /Interfaz_CAN/CAN1_MODE
- U101 pad 139: /Conexiones_extra/I2CA_SCL -> /Interfaz_CAN/CAN1_RX
- U101 pad 140: /Conexiones_extra/I2CA_SDA -> /Interfaz_CAN/CAN1_TX
- U101 pad 54: /Sensores/MAG_SCL -> /Conexiones_extra/I2CA_SCL
- U101 pad 55: /Sensores/MAG_SDA -> /Conexiones_extra/I2CA_SDA
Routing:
- net /MCU/SDMMC1_D1: track 0.00 -> 40.0 mm, vias 0 -> 1
- net /MCU/SDMMC1_D0: track 0.00 -> 35.8 mm, vias 0 -> 1
- net /MCU/SDMMC1_CK: track 0.00 -> 30.1 mm, vias 0 -> 1
- net /MCU/SDMMC1_CMD: track 0.00 -> 25.0 mm, vias 0 -> 1
- net /MCU/PF_5(EXTI5): track 0.00 -> 25.0 mm
- net /MCU/SPI5_MISO: track 0.00 -> 20.4 mm, vias 0 -> 2
- net /MCU/SDMMC1_D3: track 0.00 -> 19.8 mm, vias 0 -> 1
- net /MCU/SDMMC1_D2: track 0.00 -> 19.4 mm, vias 0 -> 1
- net /MCU/SPI5_MOSI: track 0.00 -> 17.1 mm, vias 0 -> 2
- net /MCU/SPI5_SCK: track 0.00 -> 16.7 mm
- net /MCU/OSC_OUT: track 0.00 -> 16.2 mm
- net /MCU/SPI5_CS: track 0.00 -> 14.1 mm, vias 0 -> 2
- net /MCU/OSC32_IN: track 0.00 -> 14.0 mm
- net /MCU/OSC_IN: track 0.00 -> 13.1 mm
- net /MCU/OSC32_OUT: track 0.00 -> 12.3 mm
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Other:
- board size 80 x 62.2 mm -> 308.8 x 80 mm
- copper layers 2 -> 4
